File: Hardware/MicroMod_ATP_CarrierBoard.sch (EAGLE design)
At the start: 49 parts, among them J12 SPI, J15 Dedicated, J2 JTAG, J4 USB_A_SMT_FEMALE, J6 MICROMOD-2222-C, J8 Dedicated, U5 AP7361C-33

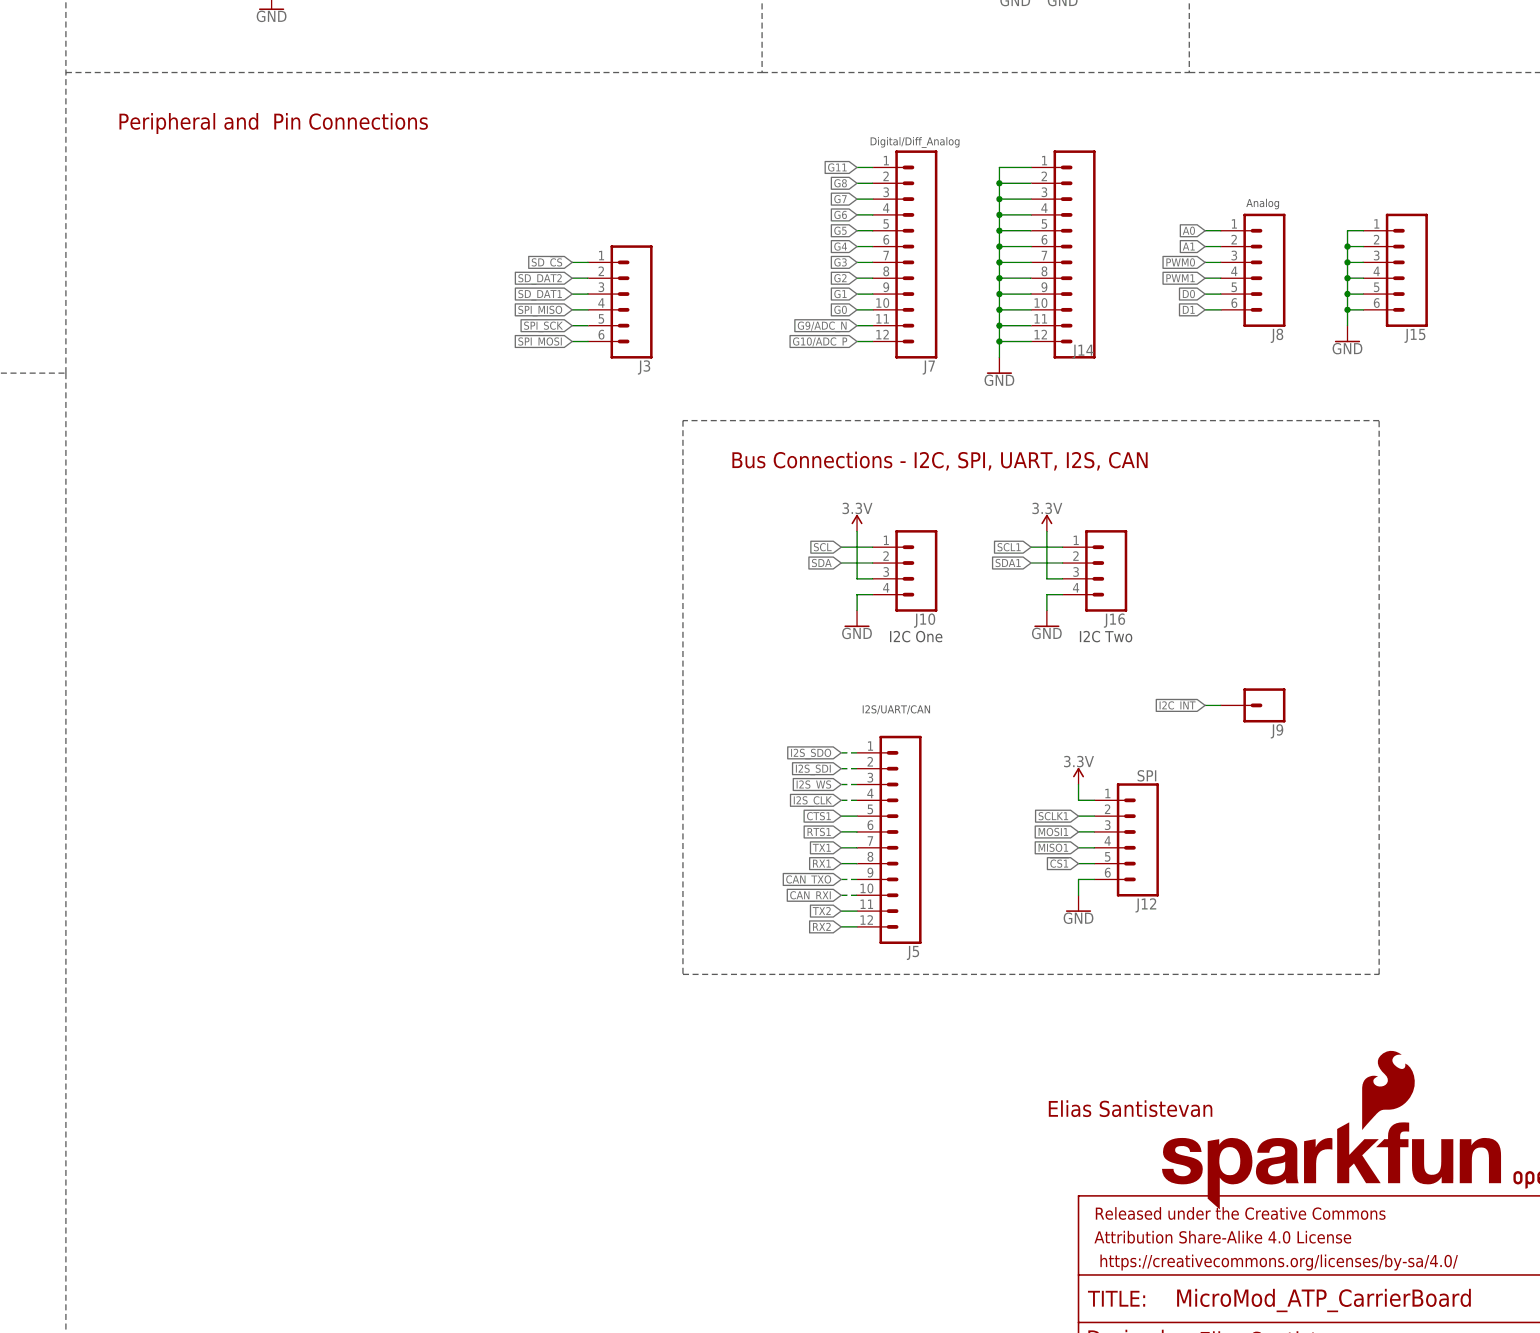
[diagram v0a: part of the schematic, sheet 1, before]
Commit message: Many headers added, netted, and placed into form factor
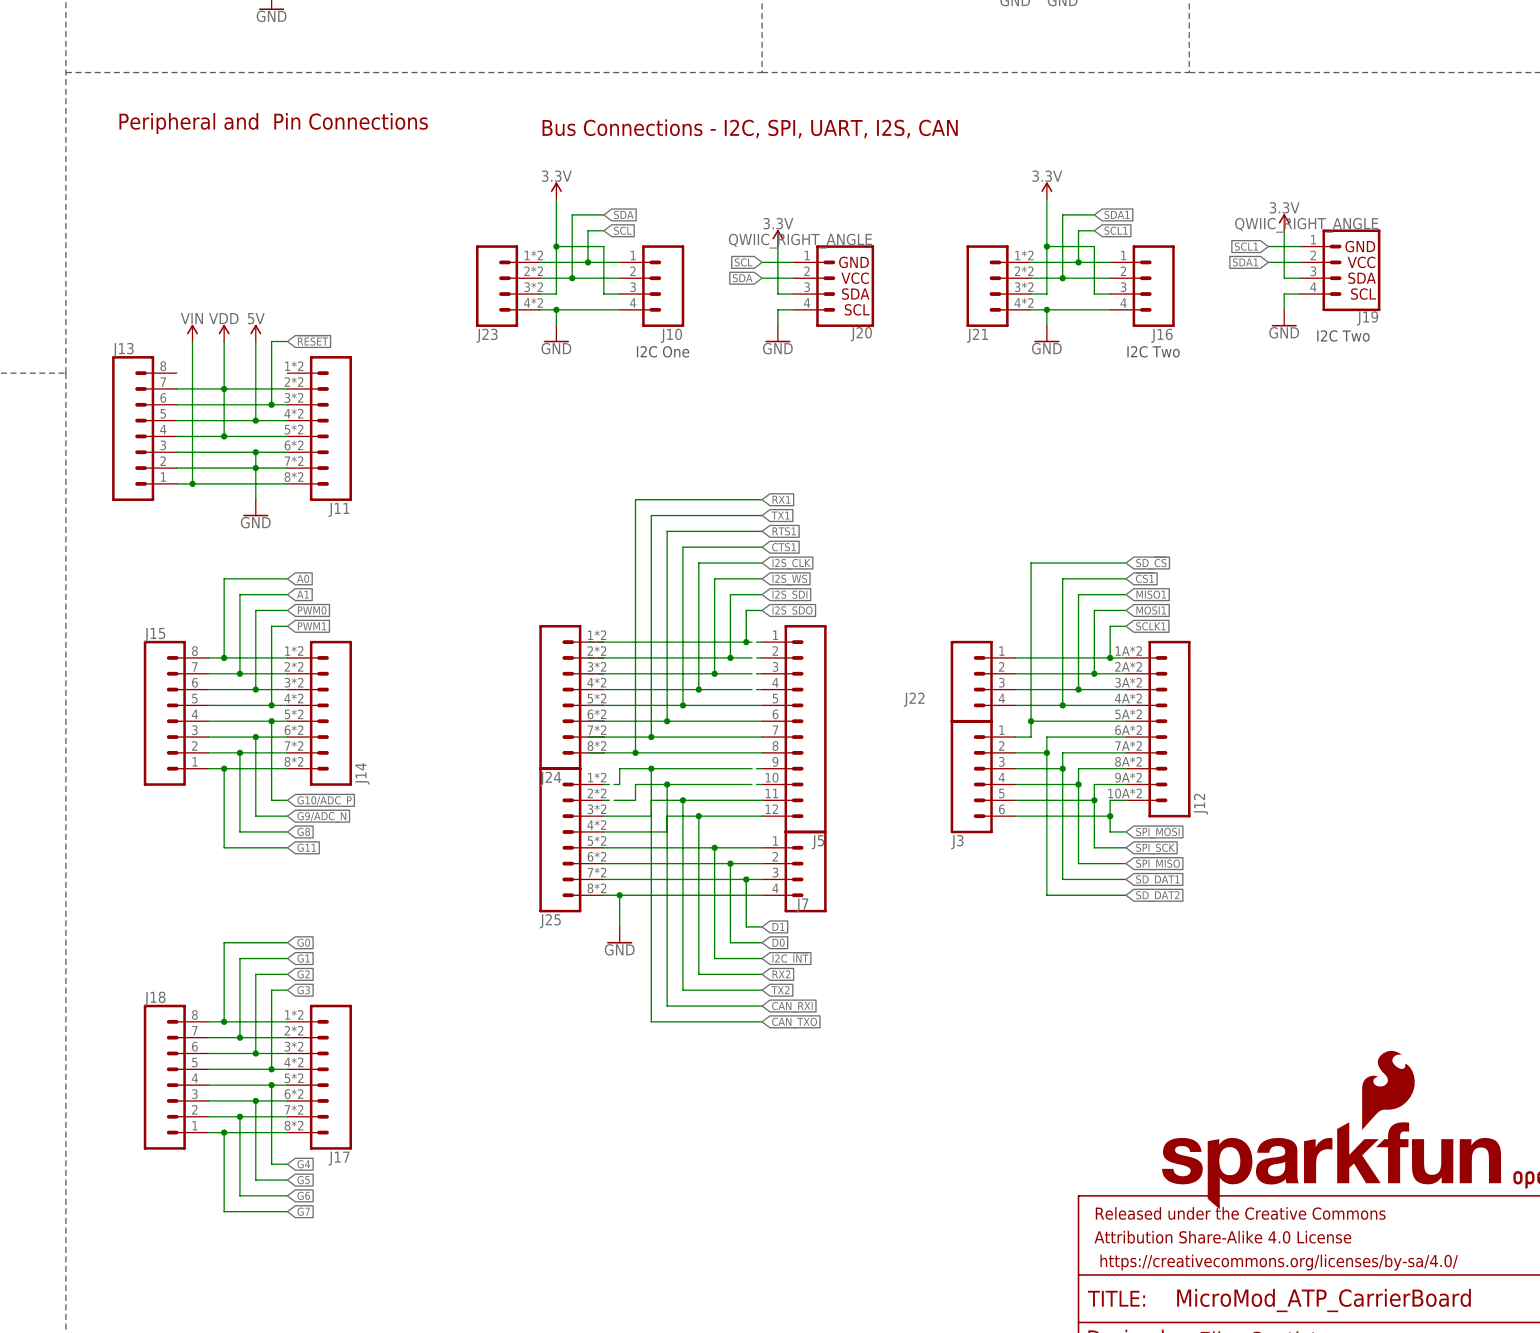
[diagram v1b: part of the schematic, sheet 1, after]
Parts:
- removed J8: Dedicated, SparkFun-Connectors:CONN_06NO_SILK_NO_POP
- removed J9: (no value), SparkFun-Connectors:CONN_01PTH_NO_SILK_YES_STOP
- added J11, J17, J24, J25: (no value), SparkFun-Connectors:CONN_08SMD-COMBO-FEMALE
- added J13, J18: (no value), SparkFun-Connectors:CONN_08NO_SILK_FEMALE_PTH
- added J19, J20: QWIIC_RIGHT_ANGLE, SparkFun-Connectors:QWIIC_CONNECTORJS-1MM
- added J21, J23: 1X04_SMD_STRAIGHT_COMBO, SparkFun-Connectors:CONN_04SMD_STRAIGHT_COMBO
- added J22: (no value), SparkFun-Connectors:CONN_041X04_NO_SILK_NO_POP
- J12: value SPI -> (none); device SparkFun-Connectors:CONN_06NO_SILK_NO_POP -> SparkFun-Connectors:CONN_10SMD_COMBO-FEMALE
- J14: device SparkFun-Connectors:CONN_12NO_SILK -> SparkFun-Connectors:CONN_08SMD-COMBO-FEMALE
- J15: value Dedicated -> (none); device SparkFun-Connectors:CONN_06NO_SILK_NO_POP -> SparkFun-Connectors:CONN_08NO_SILK_FEMALE_PTH
- J7: device SparkFun-Connectors:CONN_12NO_SILK -> SparkFun-Connectors:CONN_041X04_NO_SILK_NO_POP
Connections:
- removed net !RESET!: J2.!RESET, J6.!RESET!, S1.2
- new net !RESET: J11.3, J13.6, J2.!RESET, J6.!RESET!, S1.2
- new net 5V: J11.4, J13.5
- new net VDD: J11.2, J11.5, J13.4, J13.7
- net !CS1: now also J12.4, J22.4; no longer J12.5
- net 3.3V: now also J19.3, J20.3, J21.3, J23.3; no longer J12.1
- net A0: now also J14.1, J15.8; no longer J8.1
- net A1: now also J14.2, J15.7; no longer J8.2
- net CAN_RXI: now also J25.2
- net CAN_TXO: now also J25.1
- net CTS1: now also J24.5
- net D0: now also J25.6, J7.2; no longer J8.5
- net D1: now also J25.7, J7.3; no longer J8.6
- net G0: now also J17.1, J18.8; no longer J7.10
- net G1: now also J17.2, J18.7; no longer J7.9
- net G10/ADC_P: now also J14.5, J15.4; no longer J7.12
- net G11: now also J14.8, J15.1; no longer J7.1
- net G2: now also J17.3, J18.6; no longer J7.8
- net G3: now also J17.4, J18.5; no longer J7.7
- net G4: now also J17.5, J18.4; no longer J7.6
- net G5: now also J17.6, J18.3; no longer J7.5
- net G6: now also J17.7, J18.2; no longer J7.4
- net G7: now also J17.8, J18.1; no longer J7.3
- net G8: now also J14.7, J15.2; no longer J7.2
- net G9/ADC_N: now also J14.6, J15.3; no longer J7.11
- net GND: now also J11.6, J11.7, J13.2, J13.3, J19.4, J20.4, J21.4, J23.4, J25.8, J7.4; no longer J12.6, J14.1, J14.10, J14.11, J14.12, J14.2, J14.3, J14.4, J14.5, J14.6, J14.7, J14.8, J14.9, J15.1, J15.2, J15.3, J15.4, J15.5, J15.6
- net I2C_!INT: now also J25.5, J7.1; no longer J9.1
- net I2S_CLK: now also J24.4
- net I2S_SDI: now also J24.2
- net I2S_SDO: now also J24.1
- net I2S_WS: now also J24.3
- net MISO1: now also J12.3, J22.3; no longer J12.4
- net MOSI1: now also J12.2, J22.2; no longer J12.3
- net PWM0: now also J14.3, J15.6; no longer J8.3
- net PWM1: now also J14.4, J15.5; no longer J8.4
- net RTS1: now also J24.6
- net RX1: now also J24.8
- net RX2: now also J25.4
- net SCL: now also J20.1, J23.1
- net SCL1: now also J19.1, J21.1
- net SCLK1: now also J12.1, J22.1; no longer J12.2
- net SDA: now also J20.2, J23.2
- net SDA1: now also J19.2, J21.2
- net SD_!CS!: now also J12.5
- net SD_DAT1: now also J12.7
- net SD_DAT2: now also J12.6
- net SPI_MISO: now also J12.8
- net SPI_MOSI: now also J12.10
- net SPI_SCK: now also J12.9
- net TX1: now also J24.7
- net TX2: now also J25.3
- net VIN: now also J11.8, J13.1
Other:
- note removed: "Analog"
- note removed: "Digital/Diff_Analog"
- note removed: "I2S/UART/CAN"
- moved on the sheet: J10, J16, J3, J5

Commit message: Trace work for ATP board
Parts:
- added D2: RED, SparkFun-LED:LED-RED0603
- added J8: 1X04_SMD_STRAIGHT_COMBO, SparkFun-Connectors:CONN_041X04_NO_SILK_NO_POP
- added JP2: JUMPER-SMT_2_NC_TRACE_SILK, SparkFun-Jumpers:JUMPER-SMT_2_NC_TRACE_SILK
- added R1: 1k, SparkFun-Resistors:1KOHM-0603-1/10W-1%
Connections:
- net G10/ADC_P renamed ADC_P
- net G9/ADC_N renamed ADC_N
- new net N$1: D2.A, R1.1
- new net N$4: D2.C, JP2.2
- net !CS1: now also J12.1, J22.1; no longer J12.4, J22.4
- net 3.3V: now also R1.2
- net GND: now also J8.1, JP2.1
- net MISO1: now also J12.4, J22.4; no longer J12.3, J22.3
- net MOSI1: now also J12.3, J22.3; no longer J12.2, J22.2
- net SCLK1: now also J12.2, J22.2; no longer J12.1, J22.1
- net SPI_MOSI: now also J12.9, J3.5; no longer J12.10, J3.6
- net SPI_SCK: now also J12.10, J3.6; no longer J12.9, J3.5
- net USBHOST_N: now also J8.3
- net USBHOST_P: now also J8.2
- net V_USB: now also J8.4
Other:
- moved on the sheet: J11, J12, J13, J14, J15, J17, J18, J22, J24, J25, J3, J4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

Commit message: Adds barrel jack for power
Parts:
- removed J4: USB_A_SMT_FEMALE, SparkFun-Connectors:USB_A_SMT_FEMALE
- added C3: 47uF, SparkFun-Capacitors:47UF-POLAR-EIA3528-10V-10%
- added D3: 1A/40V/500mV, SparkFun-DiscreteSemi:DIODE-SCHOTTKY-SS14
- added IC3: LM1117, Testing:V_REG_LM1117ALT1
- added J26: POWER_JACKTOE, SparkFun-Connectors:POWER_JACKTOE
- added Q1: 2.5A/30V/105mΩ, SparkFun-DiscreteSemi:MOSFET_PCH-DMG2307L
- added R14: 715, SparkFun-Resistors:715OHM-0603-1/10W-1%
- added R15: 240, SparkFun-Resistors:240OHM-0603-1/10W-1%
- added R4: 10k, SparkFun-Resistors:10KOHM-0603-1/10W-1%
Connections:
- new net INSERT: J26.GND, Q1.G, R4.1
- new net N$15: IC3.ADJ, R14.2, R15.1
- new net PWRIN: D3.A, J26.PWR
- new net SHIELD: J1.SHLD
- net 5V: now also C1.1, C13.1, C2.+, IC3.OUT, IC3.OUT@1, Q1.S, R15.2, R4.2, R5.2, U5.IN
- net GND: now also C3.-, J26.GNDBREAK, R14.1; no longer J4.GND, J4.SHLD
- net USBHOST_N: no longer J4.D-
- net USBHOST_P: no longer J4.D+
- net VIN: now also C3.+, D3.C, IC3.IN; no longer C1.1, C13.1, C2.+, R5.2, U5.IN
- net V_USB: now also Q1.D; no longer J4.VBUS
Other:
- note added: "SWD"
- note added: "VIN Range: 7-15V"
- note removed: "JTAG"
- note removed: "This is the penny-in-the-fuse jumper. Close only if you know what you're doing."
- moved on the sheet: BT1, BYP, C1, C13, C2, C5, C6, C7, D1, D6, D7, F2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

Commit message: "Reverts" back to a time when barrel jack did not exist
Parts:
- removed C3: 47uF, SparkFun-Capacitors:47UF-POLAR-EIA3528-10V-10%
- removed D2: RED, SparkFun-LED:LED-RED0603
- removed D3: 1A/40V/500mV, SparkFun-DiscreteSemi:DIODE-SCHOTTKY-SS14
- removed IC3: LM1117, Testing:V_REG_LM1117ALT1
- removed J11: (no value), SparkFun-Connectors:CONN_08SMD-COMBO-FEMALE
- removed J13: (no value), SparkFun-Connectors:CONN_08NO_SILK_FEMALE_PTH
- removed J26: POWER_JACKTOE, SparkFun-Connectors:POWER_JACKTOE
- removed JP2: JUMPER-SMT_2_NC_TRACE_SILK, SparkFun-Jumpers:JUMPER-SMT_2_NC_TRACE_SILK
- removed Q1: 2.5A/30V/105mΩ, SparkFun-DiscreteSemi:MOSFET_PCH-DMG2307L
- removed R1: 1k, SparkFun-Resistors:1KOHM-0603-1/10W-1%
- removed R14: 715, SparkFun-Resistors:715OHM-0603-1/10W-1%
- removed R15: 240, SparkFun-Resistors:240OHM-0603-1/10W-1%
- removed R4: 10k, SparkFun-Resistors:10KOHM-0603-1/10W-1%
- added J4: USB_A_SMT_FEMALE, SparkFun-Connectors:USB_A_SMT_FEMALE
- added J9: (no value), SparkFun-Connectors:CONN_041X04_NO_SILK
- J8: device SparkFun-Connectors:CONN_041X04_NO_SILK_NO_POP -> SparkFun-Connectors:CONN_04SMD_STRAIGHT_COMBO
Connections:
- net ADC_N renamed G9/ADC_N
- net ADC_P renamed G10/ADC_P
- removed net 5V: C1.1, C13.1, C2.+, IC3.OUT, IC3.OUT@1, J11.4, J13.5, Q1.S, R15.2, R4.2, R5.2, U5.IN
- removed net INSERT: J26.GND, Q1.G, R4.1
- removed net N$1: D2.A, R1.1
- removed net N$15: IC3.ADJ, R14.2, R15.1
- removed net N$4: D2.C, JP2.2
- removed net PWRIN: D3.A, J26.PWR
- removed net SHIELD: J1.SHLD
- removed net VDD: J11.2, J11.5, J13.4, J13.7
- net !CS1: now also J12.4, J22.4; no longer J12.1, J22.1
- net !RESET: no longer J11.3, J13.6
- net 3.3V: no longer R1.2
- net GND: now also J4.GND, J4.SHLD; no longer C3.-, J11.6, J11.7, J13.2, J13.3, J26.GNDBREAK, J8.1, JP2.1, R14.1
- net MISO1: now also J12.3, J22.3; no longer J12.4, J22.4
- net MOSI1: now also J12.2, J22.2; no longer J12.3, J22.3
- net SCLK1: now also J12.1, J22.1; no longer J12.2, J22.2
- net SPI_MOSI: now also J12.10, J3.6; no longer J12.9, J3.5
- net SPI_SCK: now also J12.9, J3.5; no longer J12.10, J3.6
- net USBHOST_N: now also J4.D-; no longer J8.3
- net USBHOST_P: now also J4.D+; no longer J8.2
- net VIN: now also C1.1, C13.1, C2.+, R5.2, U5.IN; no longer C3.+, D3.C, IC3.IN, J11.8, J13.1
- net V_USB: now also J4.VBUS; no longer J8.4, Q1.D
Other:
- note added: "JTAG"
- note added: "This is the penny-in-the-fuse jumper. Close only if you know what you're doing."
- note removed: "SWD"
- note removed: "VIN Range: 7-15V"
- moved on the sheet: BT1, BYP, C1, C13, C2, C5, C6, C7, D1, D6, D7, F2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

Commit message: Shrinks board, adds routing
* board is now 2 x 3 roughly
* Added a longer header for MCLK and GND -> went from 10-12 pin
*  Routed SPI, QSPI, and I2S
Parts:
- removed J3: (no value), SparkFun-Connectors:CONN_06NO_SILK_NO_POP
- removed JP1: JUMPER-SMT_3_2-NC_TRACE_SILK, SparkFun-Jumpers:JUMPER-SMT_3_2-NC_TRACE_SILK
- removed LOGO1: SFE_LOGO_NAME_FLAME.1_INCH, SparkFun-Aesthetics:SFE_LOGO_NAME_FLAME.1_INCH
- added J11: (no value), SparkFun-Connectors:CONN_041X04_NO_SILK_NO_POP
- added J13: (no value), SparkFun-Connectors:CONN_08NO_SILK_DNP
- J12: device SparkFun-Connectors:CONN_10SMD_COMBO-FEMALE -> SparkFun-Connectors:CONN_12SMD_COMBINED
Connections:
- removed net N$2: JP1.3, R10.1
- removed net N$3: JP1.1, R9.2
- new net !RESET!: J8.3, J9.3
- net !CS1: now also J12.1, J22.1; no longer J12.4, J22.4
- net 3.3V: now also J8.2, J9.2
- net GND: now also J11.4, J12.11, J13.2, J8.4, J9.4
- net MCLK: now also J12.12, J13.1
- net MISO1: now also J12.4, J22.4; no longer J12.3, J22.3
- net MOSI1: now also J12.3, J22.3; no longer J12.2, J22.2
- net SCLK1: now also J12.2, J22.2; no longer J12.1, J22.1
- net SD_!CS!: now also J13.8; no longer J3.1
- net SD_DAT1: now also J13.6; no longer J3.3
- net SD_DAT2: now also J13.7; no longer J3.2
- net SPI_MISO: now also J13.5; no longer J3.4
- net SPI_MOSI: now also J12.9, J13.4; no longer J12.10, J3.6
- net SPI_SCK: now also J12.10, J13.3; no longer J12.9, J3.5
- net USBHOST_N: now also J11.2
- net USBHOST_P: now also J11.3
- net VIN: now also J8.1, J9.1
- net VIN/3: now also R10.1, R9.2; no longer JP1.2
- net V_USB: now also J11.1
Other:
- moved on the sheet: J8, J9, R10, R9
